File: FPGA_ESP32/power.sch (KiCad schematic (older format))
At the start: 1 part

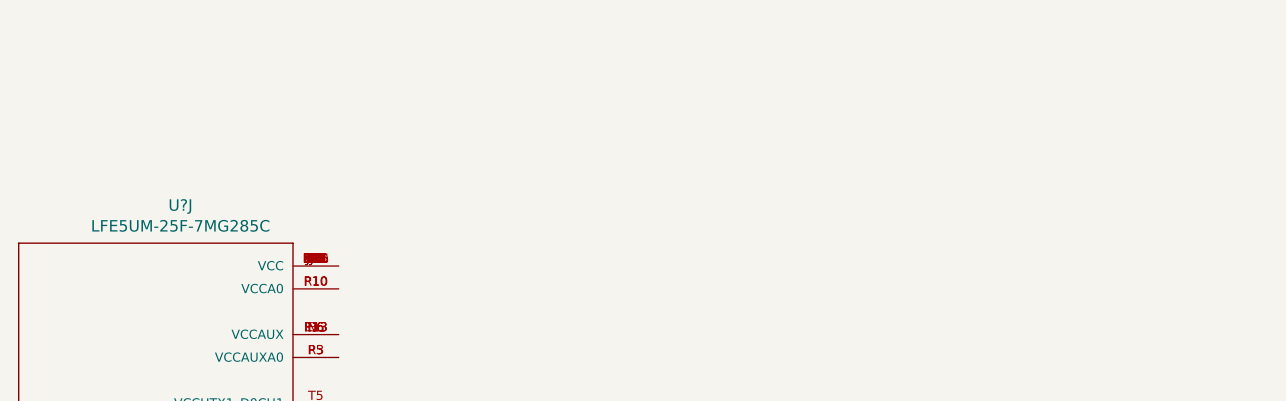
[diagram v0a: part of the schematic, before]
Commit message: FPGA_ESP32 : add header + esp32 with SDIO
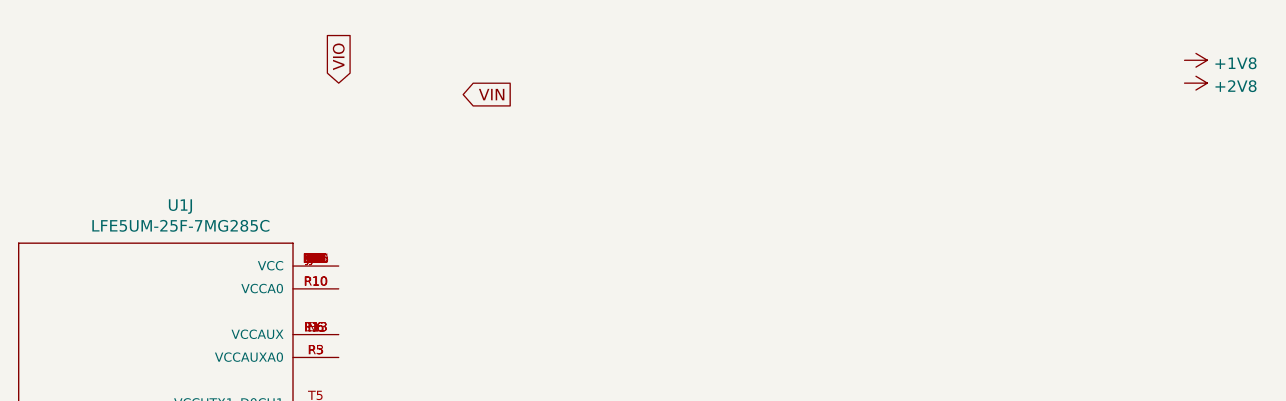
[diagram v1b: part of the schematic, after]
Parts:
- U1: renamed from U?; footprint BGA285N50P18X18_1000X1000X130N -> footprints:BGA285N50P18X18_1000X1000X130N
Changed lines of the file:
@@
 P 2000 3700
 AR Path="/5BC231CE/5EED90AF" Ref="U?"  Part="10"
-AR Path="/5BC231CB/5EED90AF" Ref="U?"  Part="10"
-F 0 "U?" H 2108 4565 50  0000 C CNN
+AR Path="/5BC231CB/5EED90AF" Ref="U1"  Part="10"
+F 0 "U1" H 2108 4565 50  0000 C CNN
 F 1 "LFE5UM-25F-7MG285C" H 2108 4474 50  0000 C CNN
-F 2 "BGA285N50P18X18_1000X1000X130N" H 2000 3700 50  0001 L BNN
+F 2 "footprints:BGA285N50P18X18_1000X1000X130N" H 2000 3700 50  0001 L BNN
 F 3 "1.3" H 2000 3700 50  0001 L BNN
 F 4 "18.0" H 2000 3700 50  0001 L BNN "Field4"
@@
 	1    0    0    -1
 $EndComp
+Text GLabel 2800 2300 1    50   Input ~ 0
+VIO
+$Comp
+L power:+1V8 #PWR?
+U 1 1 5F18FF71
+P 6500 2200
+AR Path="/5BC231CE/5F18FF71" Ref="#PWR?"  Part="1"
+AR Path="/5BC231CB/5F18FF71" Ref="#PWR?"  Part="1"
+F 0 "#PWR?" H 6500 2050 50  0001 C CNN
+F 1 "+1V8" V 6515 2328 50  0000 L CNN
+F 2 "" H 6500 2200 50  0001 C CNN
+F 3 "" H 6500 2200 50  0001 C CNN
+	1    6500 2200
+	0    1    1    0
+$EndComp
+$Comp
+L power:+2V8 #PWR?
+U 1 1 5F192EE4
+P 6500 2300
+AR Path="/5BC231CE/5F192EE4" Ref="#PWR?"  Part="1"
+AR Path="/5BC231CB/5F192EE4" Ref="#PWR?"  Part="1"
+F 0 "#PWR?" H 6500 2150 50  0001 C CNN
+F 1 "+2V8" V 6515 2428 50  0000 L CNN
+F 2 "" H 6500 2300 50  0001 C CNN
+F 3 "" H 6500 2300 50  0001 C CNN
+	1    6500 2300
+	0    1    1    0
+$EndComp
+Text GLabel 3550 2350 0    50   Output ~ 0
+VIN
 $EndSCHEMATC

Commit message: FPGA_ESP32 : add camera, change header position
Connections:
- net labels added: +1V1, +2V5, GND
- wire segments 0 -> 7
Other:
- note added: "1V1 Reg"
- note added: "1V8 Reg"
- note added: "2V5 Reg"
- note added: "2V8 Reg\nTODO : Check if 2V5 is enought for OV5640"
- note added: "3V3 Reg"
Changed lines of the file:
@@
 Text GLabel 3550 2350 0    50   Output ~ 0
 VIN
+$Comp
+L power:+1V1 #PWR0101
+U 1 1 5EEA1D15
+P 2800 3150
+F 0 "#PWR0101" H 2800 3000 50  0001 C CNN
+F 1 "+1V1" V 2815 3278 50  0000 L CNN
+F 2 "" H 2800 3150 50  0001 C CNN
+F 3 "" H 2800 3150 50  0001 C CNN
+	1    2800 3150
+	0    1    1    0
+$EndComp
+$Comp
+L power:+2V5 #PWR0102
+U 1 1 5EEA3EF8
+P 2800 3450
+F 0 "#PWR0102" H 2800 3300 50  0001 C CNN
+F 1 "+2V5" V 2815 3578 50  0000 L CNN
+F 2 "" H 2800 3450 50  0001 C CNN
+F 3 "" H 2800 3450 50  0001 C CNN
+	1    2800 3450
+	0    1    1    0
+$EndComp
+$Comp
+L power:+1V1 #PWR0103
+U 1 1 5EEA6B1A
+P 2800 3700
+F 0 "#PWR0103" H 2800 3550 50  0001 C CNN
+F 1 "+1V1" V 2815 3828 50  0000 L CNN
+F 2 "" H 2800 3700 50  0001 C CNN
+F 3 "" H 2800 3700 50  0001 C CNN
+	1    2800 3700
+	0    1    1    0
+$EndComp
+Wire Wire Line
+	2800 3700 2800 3800
+Connection ~ 2800 3700
+Connection ~ 2800 3800
+Wire Wire Line
+	2800 3800 2800 3900
+Connection ~ 2800 3900
+Wire Wire Line
+	2800 3900 2800 4000
+$Comp
+L power:GND #PWR0104
+U 1 1 5EEA772E
+P 2800 4300
+F 0 "#PWR0104" H 2800 4050 50  0001 C CNN
+F 1 "GND" V 2805 4172 50  0000 R CNN
+F 2 "" H 2800 4300 50  0001 C CNN
+F 3 "" H 2800 4300 50  0001 C CNN
+	1    2800 4300
+	0    -1   -1   0
+$EndComp
+Wire Wire Line
+	2800 3100 2800 3150
+Connection ~ 2800 3150
+Wire Wire Line
+	2800 3150 2800 3200
+Wire Wire Line
+	2800 3400 2800 3450
+Connection ~ 2800 3450
+Wire Wire Line
+	2800 3450 2800 3500
+Text Notes 5000 2900 0    50   ~ 0
+1V1 Reg
+$Comp
+L power:+1V1 #PWR0105
+U 1 1 5EEC8772
+P 5500 3200
+F 0 "#PWR0105" H 5500 3050 50  0001 C CNN
+F 1 "+1V1" V 5515 3328 50  0000 L CNN
+F 2 "" H 5500 3200 50  0001 C CNN
+F 3 "" H 5500 3200 50  0001 C CNN
+	1    5500 3200
+	0    1    1    0
+$EndComp
+Text Notes 5000 3900 0    50   ~ 0
+1V8 Reg
+Text Notes 5050 4850 0    50   ~ 0
+2V5 Reg
+Text Notes 5050 5800 0    50   ~ 0
+3V3 Reg
+Text Notes 5050 6600 0    50   ~ 0
+2V8 Reg\nTODO : Check if 2V5 is enought for OV5640
 $EndSCHEMATC
